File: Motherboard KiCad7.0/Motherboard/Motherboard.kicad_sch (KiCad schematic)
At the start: 92 parts, among them J1 USB_B_Micro, J10 430450200, J11 430450200, J12 430450200, J2 SWD_01x04_Pin, J3 430450200, J4 430450200, J5 B04B-XASK-1, J6 430450200, J7 430450200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

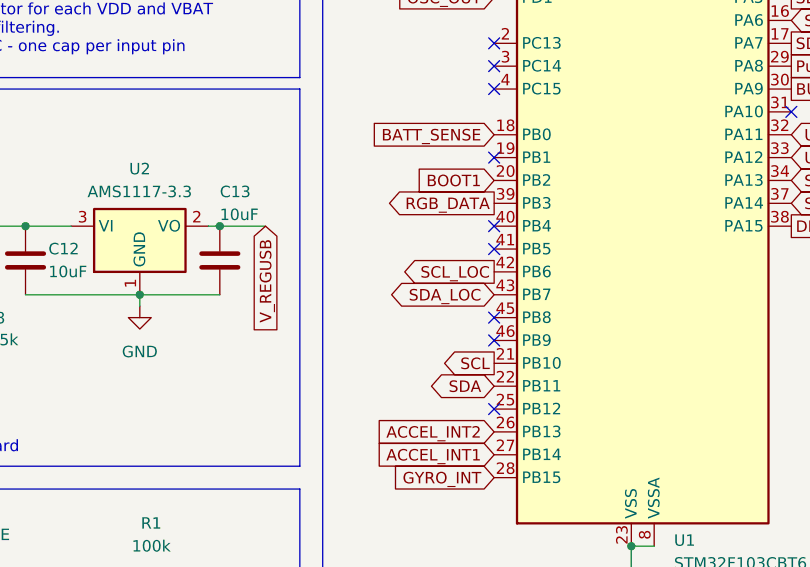
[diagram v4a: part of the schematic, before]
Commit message: Added pull-up resistors to I2C
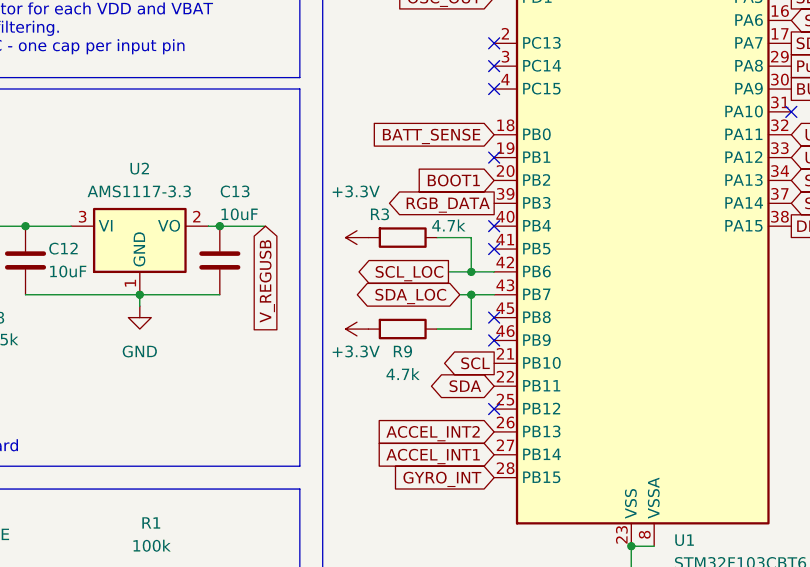
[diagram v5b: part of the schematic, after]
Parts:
- added R3, R9: 4.7k, Resistor_SMD:R_0603_1608Metric, symbol Device:R
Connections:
- net +3.3V: now also R3.2, R9.2
- net SCL_LOC: now also R3.1
- net SDA_LOC: now also R9.1
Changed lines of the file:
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@@
   (junction (at 262.89 31.75) (diameter 0) (color 0 0 0 0)
   )
+  (junction (at 300.99 82.55) (diameter 0) (color 0 0 0 0)
+  )
   (junction (at 317.5 189.23) (diameter 0) (color 0 0 0 0)
   )
@@
   (junction (at 193.04 172.72) (diameter 0) (color 0 0 0 0)
   )
+  (junction (at 300.99 85.09) (diameter 0) (color 0 0 0 0)
+  )
   (junction (at 168.91 243.84) (diameter 0) (color 0 0 0 0)
   )
@@
     (stroke (width 0) (type default))
   )
+  (wire (pts (xy 297.18 88.9) (xy 300.99 88.9))
+    (stroke (width 0) (type default))
+  )
   (wire (pts (xy 378.46 58.42) (xy 386.08 58.42))
     (stroke (width 0) (type default))
@@
     (stroke (width 0) (type default))
   )
+  (wire (pts (xy 299.72 85.09) (xy 300.99 85.09))
+    (stroke (width 0) (type default))
+  )
   (wire (pts (xy 317.5 189.23) (xy 317.5 191.77))
     (stroke (width 0) (type default))
@@
     (stroke (width 0) (type default))
   )
+  (wire (pts (xy 298.45 82.55) (xy 300.99 82.55))
+    (stroke (width 0) (type default))
+  )
   (wire (pts (xy 311.15 134.62) (xy 306.07 134.62))
     (stroke (width 0) (type default))
@@
     (stroke (width 0) (type default))
   )
+  (wire (pts (xy 300.99 82.55) (xy 303.53 82.55))
+    (stroke (width 0) (type default))
+  )
   (wire (pts (xy 111.76 62.23) (xy 111.76 63.5))
     (stroke (width 0) (type default))
@@
     (stroke (width 0) (type default))
   )
+  (wire (pts (xy 297.18 78.74) (xy 300.99 78.74))
+    (stroke (width 0) (type default))
+  )
   (wire (pts (xy 171.45 68.58) (xy 173.99 68.58))
     (stroke (width 0) (type default))
@@
     (stroke (width 0) (type default))
   )
+  (wire (pts (xy 300.99 88.9) (xy 300.99 85.09))
+    (stroke (width 0) (type default))
+  )
   (wire (pts (xy 384.81 85.09) (xy 386.08 85.09))
     (stroke (width 0) (type default))
@@
     (stroke (width 0) (type default))
   )
+  (wire (pts (xy 300.99 85.09) (xy 303.53 85.09))
+    (stroke (width 0) (type default))
+  )
   (polyline (pts (xy 96.52 60.96) (xy 53.34 60.96))
     (stroke (width 0) (type solid))
@@
     (stroke (width 0) (type default))
   )
+  (wire (pts (xy 300.99 78.74) (xy 300.99 82.55))
+    (stroke (width 0) (type default))
+  )
   (wire (pts (xy 185.42 172.72) (xy 193.04 172.72))
     (stroke (width 0) (type default))
@@
     (effects (font (size 1.27 1.27)) (justify left bottom))
   )
-  (global_label "SCL_LOC" (shape output) (at 303.53 82.55 180) (fields_autoplaced)
+  (global_label "SCL_LOC" (shape output) (at 298.45 82.55 180) (fields_autoplaced)
     (effects (font (size 1.27 1.27)) (justify right))
-    (property "Intersheetrefs" "${INTERSHEET_REFS}" (at 292.441 82.55 0)
+    (property "Intersheetrefs" "${INTERSHEET_REFS}" (at 287.361 82.55 0)
       (effects (font (size 1.27 1.27)) (justify right) hide)
     )
@@
     )
   )
-  (global_label "SDA_LOC" (shape bidirectional) (at 303.53 85.09 180) (fields_autoplaced)
+  (global_label "SDA_LOC" (shape bidirectional) (at 299.72 85.09 180) (fields_autoplaced)
     (effects (font (size 1.27 1.27)) (justify right))
-    (property "Intersheetrefs" "${INTERSHEET_REFS}" (at 291.2692 85.09 0)
+    (property "Intersheetrefs" "${INTERSHEET_REFS}" (at 287.4592 85.09 0)
       (effects (font (size 1.27 1.27)) (justify right) hide)
     )
@@
     )
   )
+  (symbol (lib_id "Device:R") (at 293.37 78.74 270) (unit 1)
+    (in_bom yes) (on_board yes) (dnp no)
+    (property "Reference" "R3" (at 290.83 76.2 90)
+      (effects (font (size 1.27 1.27)))
+    )
+    (property "Value" "4.7k" (at 298.45 77.47 90)
+      (effects (font (size 1.27 1.27)))
+    )
+    (property "Footprint" "Resistor_SMD:R_0603_1608Metric" (at 293.37 76.962 90)
+      (effects (font (size 1.27 1.27)) hide)
+    )
+    (property "Datasheet" "~" (at 293.37 78.74 0)
+      (effects (font (size 1.27 1.27)) hide)
+    )
+    (pin "1")
+    (pin "2")
+    (instances
+      (project "Motherboard"
+        (path "/6c6aab7b-9fc7-4161-8073-41667e18c629"
+          (reference "R3") (unit 1)
+        )
+      )
+    )
+  )
+  (symbol (lib_id "power:+3.3V") (at 289.56 78.74 90) (unit 1)
+    (in_bom yes) (on_board yes) (dnp no)
+    (property "Reference" "#PWR068" (at 293.37 78.74 0)
+      (effects (font (size 1.27 1.27)) hide)
+    )
+    (property "Value" "+3.3V" (at 290.83 73.66 90)
+      (effects (font (size 1.27 1.27)) (justify left))
+    )
+    (property "Footprint" "" (at 289.56 78.74 0)
+      (effects (font (size 1.27 1.27)) hide)
+    )
+    (property "Datasheet" "" (at 289.56 78.74 0)
+      (effects (font (size 1.27 1.27)) hide)
+    )
+    (pin "1")
+    (instances
+      (project "Motherboard"
+        (path "/6c6aab7b-9fc7-4161-8073-41667e18c629"
+          (reference "#PWR068") (unit 1)
+        )
+      )
+    )
+  )
   (symbol (lib_id "Diode:1N5819WS") (at 378.46 82.55 270) (unit 1)
     (in_bom yes) (on_board yes) (dnp no)
@@
     )
   )
+  (symbol (lib_id "power:+3.3V") (at 289.56 88.9 90) (unit 1)
+    (in_bom yes) (on_board yes) (dnp no)
+    (property "Reference" "#PWR069" (at 293.37 88.9 0)
+      (effects (font (size 1.27 1.27)) hide)
+    )
+    (property "Value" "+3.3V" (at 290.83 91.44 90)
+      (effects (font (size 1.27 1.27)) (justify left))
+    )
+    (property "Footprint" "" (at 289.56 88.9 0)
+      (effects (font (size 1.27 1.27)) hide)
+    )
+    (property "Datasheet" "" (at 289.56 88.9 0)
+      (effects (font (size 1.27 1.27)) hide)
+    )
+    (pin "1")
+    (instances
+      (project "Motherboard"
+        (path "/6c6aab7b-9fc7-4161-8073-41667e18c629"
+          (reference "#PWR069") (unit 1)
+        )
+      )
+    )
+  )
   (symbol (lib_id "power:GND") (at 389.89 99.06 90) (unit 1)
     (in_bom yes) (on_board yes) (dnp no) (fields_autoplaced)
@@
         )
       )
+    )
+  )
+  (symbol (lib_id "Device:R") (at 293.37 88.9 270) (unit 1)
+    (in_bom yes) (on_board yes) (dnp no)
+    (property "Reference" "R9" (at 293.37 91.44 90)
+      (effects (font (size 1.27 1.27)))
+    )
+    (property "Value" "4.7k" (at 293.37 93.98 90)
+      (effects (font (size 1.27 1.27)))
+    )
+    (property "Footprint" "Resistor_SMD:R_0603_1608Metric" (at 293.37 87.122 90)
+      (effects (font (size 1.27 1.27)) hide)
+    )
+    (property "Datasheet" "~" (at 293.37 88.9 0)
+      (effects (font (size 1.27 1.27)) hide)
+    )
+    (pin "1")
+    (pin "2")
+    (instances
+      (project "Motherboard"
+        (path "/6c6aab7b-9fc7-4161-8073-41667e18c629"
+          (reference "R9") (unit 1)
+        )
+      )

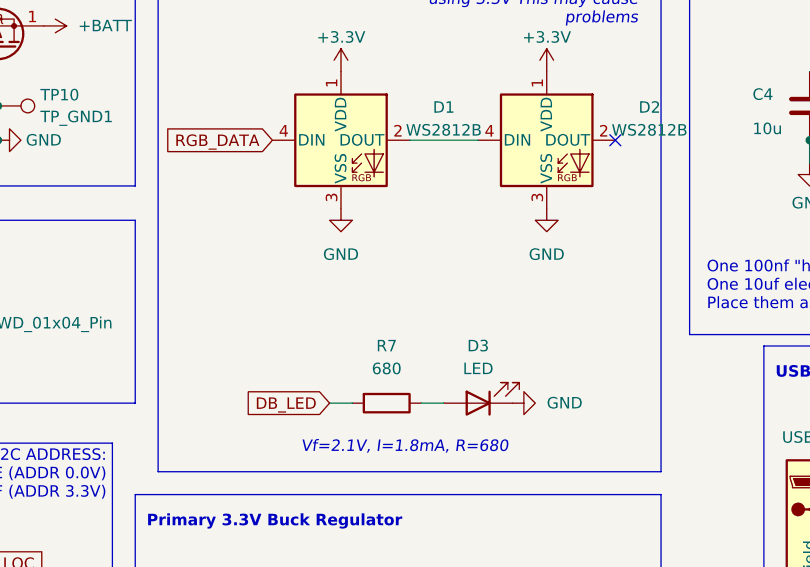
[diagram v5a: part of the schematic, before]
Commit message: Added power LED
Added power LED and part number for I2C PU resistors
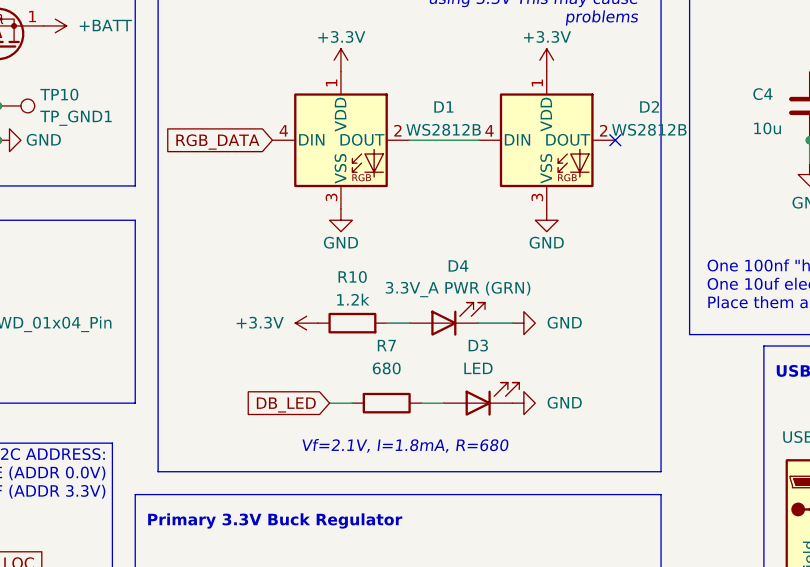
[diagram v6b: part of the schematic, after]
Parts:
- added D4: 3.3V_A PWR (GRN), LED_SMD:LED_0805_2012Metric, symbol Device:LED
- added R10: 1.2k, Resistor_SMD:R_0603_1608Metric, symbol Device:R
- R3, R9: LCSC (none) -> C23162
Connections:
- net +3.3V: now also R10.1
- net GND: now also D4.1 (K)
- new net: D4.2 (A), R10.2
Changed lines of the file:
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@@
     (stroke (width 0) (type default))
   )
+  (wire (pts (xy 177.8 59.69) (xy 180.34 59.69))
+    (stroke (width 0) (type default))
+  )
   (wire (pts (xy 64.77 33.02) (xy 64.77 36.83))
     (stroke (width 0) (type default))
@@
     (stroke (width 0) (type default))
   )
+  (wire (pts (xy 187.96 59.69) (xy 191.77 59.69))
+    (stroke (width 0) (type default))
+  )
   (wire (pts (xy 378.46 135.89) (xy 384.81 135.89))
     (stroke (width 0) (type default))
@@
       (effects (font (size 1.27 1.27)) hide)
     )
+    (property "LCSC" "C23162" (at 293.37 78.74 90)
+      (effects (font (size 1.27 1.27)) hide)
+    )
     (pin "1")
     (pin "2")
@@
   )
   (symbol (lib_id "power:GND") (at 172.72 46.99 0) (unit 1)
-    (in_bom yes) (on_board yes) (dnp no) (fields_autoplaced)
+    (in_bom yes) (on_board yes) (dnp no)
     (property "Reference" "#PWR063" (at 172.72 53.34 0)
       (effects (font (size 1.27 1.27)) hide)
     )
-    (property "Value" "GND" (at 172.72 52.07 0)
+    (property "Value" "GND" (at 172.72 50.8 0)
       (effects (font (size 1.27 1.27)))
     )
@@
   )
   (symbol (lib_id "power:GND") (at 195.58 46.99 0) (unit 1)
-    (in_bom yes) (on_board yes) (dnp no) (fields_autoplaced)
+    (in_bom yes) (on_board yes) (dnp no)
     (property "Reference" "#PWR010" (at 195.58 53.34 0)
       (effects (font (size 1.27 1.27)) hide)
     )
-    (property "Value" "GND" (at 195.58 52.07 0)
+    (property "Value" "GND" (at 195.58 50.8 0)
       (effects (font (size 1.27 1.27)))
     )
@@
     )
   )
+  (symbol (lib_id "Device:R") (at 173.99 59.69 90) (unit 1)
+    (in_bom yes) (on_board yes) (dnp no)
+    (property "Reference" "R10" (at 173.99 54.61 90)
+      (effects (font (size 1.27 1.27)))
+    )
+    (property "Value" "1.2k" (at 173.99 57.15 90)
+      (effects (font (size 1.27 1.27)))
+    )
+    (property "Footprint" "Resistor_SMD:R_0603_1608Metric" (at 173.99 61.468 90)
+      (effects (font (size 1.27 1.27)) hide)
+    )
+    (property "Datasheet" "~" (at 173.99 59.69 0)
+      (effects (font (size 1.27 1.27)) hide)
+    )
+    (property "LCSC" "C22765" (at 173.99 59.69 0)
+      (effects (font (size 1.27 1.27)) hide)
+    )
+    (pin "1")
+    (pin "2")
+    (instances
+      (project "Motherboard"
+        (path "/6c6aab7b-9fc7-4161-8073-41667e18c629"
+          (reference "R10") (unit 1)
+        )
+      )
+    )
+  )
   (symbol (lib_id "Device:R") (at 377.19 34.29 270) (unit 1)
     (in_bom yes) (on_board yes) (dnp no) (fields_autoplaced)
@@
       (effects (font (size 1.27 1.27)) hide)
     )
+    (property "LCSC" "C23162" (at 293.37 88.9 90)
+      (effects (font (size 1.27 1.27)) hide)
+    )
     (pin "1")
     (pin "2")
@@
     )
   )
+  (symbol (lib_id "power:GND") (at 191.77 59.69 90) (unit 1)
+    (in_bom yes) (on_board yes) (dnp no) (fields_autoplaced)
+    (property "Reference" "#PWR070" (at 198.12 59.69 0)
+      (effects (font (size 1.27 1.27)) hide)
+    )
+    (property "Value" "GND" (at 195.58 59.69 90)
+      (effects (font (size 1.27 1.27)) (justify right))
+    )
+    (property "Footprint" "" (at 191.77 59.69 0)
+      (effects (font (size 1.27 1.27)) hide)
+    )
+    (property "Datasheet" "" (at 191.77 59.69 0)
+      (effects (font (size 1.27 1.27)) hide)
+    )
+    (pin "1")
+    (instances
+      (project "Motherboard"
+        (path "/6c6aab7b-9fc7-4161-8073-41667e18c629"
+          (reference "#PWR070") (unit 1)
+        )
+      )
+    )
+  )
   (symbol (lib_id "power:+BATT") (at 372.11 134.62 0) (unit 1)
     (in_bom yes) (on_board yes) (dnp no)
@@
     )
   )
+  (symbol (lib_id "power:+3.3V") (at 170.18 59.69 90) (unit 1)
+    (in_bom yes) (on_board yes) (dnp no) (fields_autoplaced)
+    (property "Reference" "#PWR071" (at 173.99 59.69 0)
+      (effects (font (size 1.27 1.27)) hide)
+    )
+    (property "Value" "+3.3V" (at 166.37 59.69 90)
+      (effects (font (size 1.27 1.27)) (justify left))
+    )
+    (property "Footprint" "" (at 170.18 59.69 0)
+      (effects (font (size 1.27 1.27)) hide)
+    )
+    (property "Datasheet" "" (at 170.18 59.69 0)
+      (effects (font (size 1.27 1.27)) hide)
+    )
+    (pin "1")
+    (instances
+      (project "Motherboard"
+        (path "/6c6aab7b-9fc7-4161-8073-41667e18c629"
+          (reference "#PWR071") (unit 1)
+        )
+      )
+    )
+  )
   (symbol (lib_id "power:GND") (at 179.07 207.01 90) (unit 1)
     (in_bom yes) (on_board yes) (dnp no) (fields_autoplaced)
@@
         )
       )
+    )
+  )
+  (symbol (lib_id "Device:LED") (at 184.15 59.69 180) (unit 1)
+    (in_bom yes) (on_board yes) (dnp no) (fields_autoplaced)
+    (property "Reference" "D4" (at 185.7375 53.3867 0)
+      (effects (font (size 1.27 1.27)))
+    )
+    (property "Value" "3.3V_A PWR (GRN)" (at 185.7375 55.8109 0)
+      (effects (font (size 1.27 1.27)))
+    )
+    (property "Footprint" "LED_SMD:LED_0805_2012Metric" (at 184.15 59.69 0)
+      (effects (font (size 1.27 1.27)) hide)
+    )
+    (property "Datasheet" "~" (at 184.15 59.69 0)
+      (effects (font (size 1.27 1.27)) hide)
+    )
+    (property "LCSC" "C2297" (at 184.15 59.69 0)
+      (effects (font (size 1.27 1.27)) hide)
+    )
+    (pin "1")
+    (pin "2")
+    (instances
+      (project "Motherboard"
+        (path "/6c6aab7b-9fc7-4161-8073-41667e18c629"
+          (reference "D4") (unit 1)
+        )
+      )

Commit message: Updated part number for JST connector
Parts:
- J5: Digikey 455-B04B-XASK-1-ND -> (none); LCSC (none) -> C264994
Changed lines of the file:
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@@
       (effects (font (size 1.27 1.27) italic) hide)
     )
-    (property "Digikey" "455-B04B-XASK-1-ND" (at 267.97 175.26 0)
+    (property "LCSC" "C264994" (at 267.97 175.26 0)
       (effects (font (size 1.27 1.27)) hide)
     )
